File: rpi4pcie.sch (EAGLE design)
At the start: 88 parts

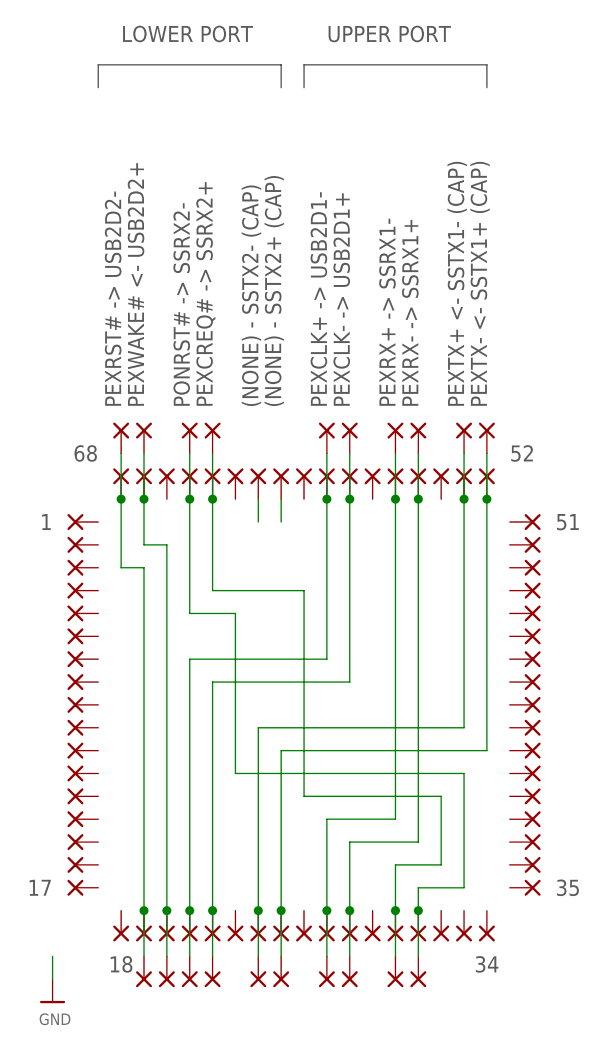
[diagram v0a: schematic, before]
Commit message: Remove extra pads from PCB for fab
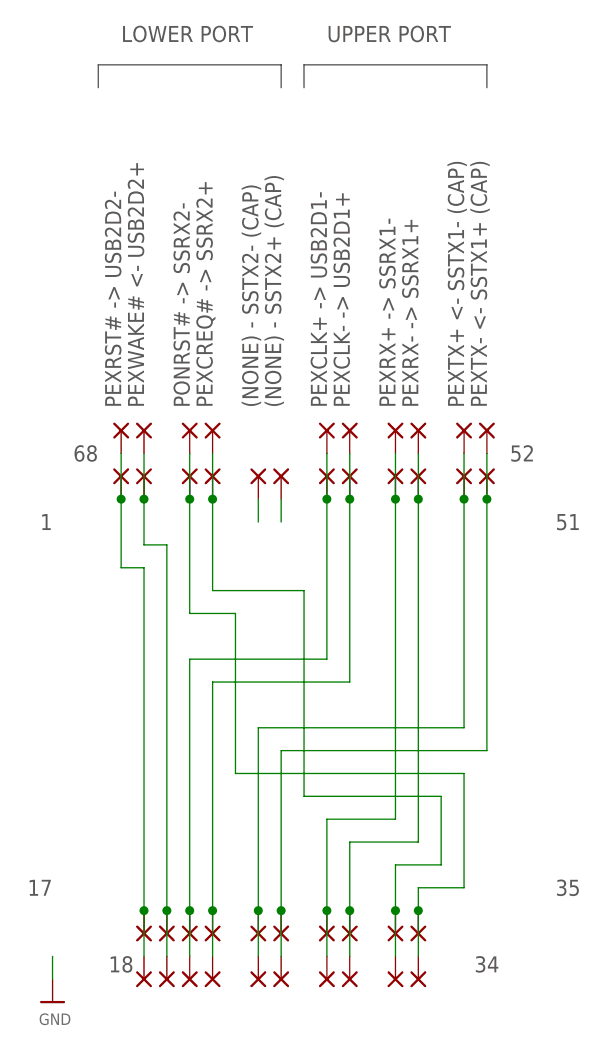
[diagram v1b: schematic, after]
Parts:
- removed PAD1, PAD10, PAD11, PAD12, PAD13, PAD14, PAD15, PAD16, PAD17, PAD18, PAD2, PAD23, PAD26, PAD29, PAD3, PAD32, PAD33, PAD34, PAD35, PAD36, PAD37, PAD38, PAD39, PAD4, PAD40, PAD41, PAD42, PAD43, PAD44, PAD45, PAD46, PAD47, PAD48, PAD49, PAD5, PAD50, PAD51, PAD54, PAD57, PAD6, PAD60, PAD63, PAD66, PAD7, PAD8, PAD9: PADQFN-0.4, zak:PADQFN-0.4
